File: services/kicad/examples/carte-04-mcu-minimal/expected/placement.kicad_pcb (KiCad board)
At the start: 2 copper layers, 60 x 45 mm, 15 parts, among them J1 IN_5V, J2 SWD, U1 STM32F103C8T6, U2 AMS1117-3.3

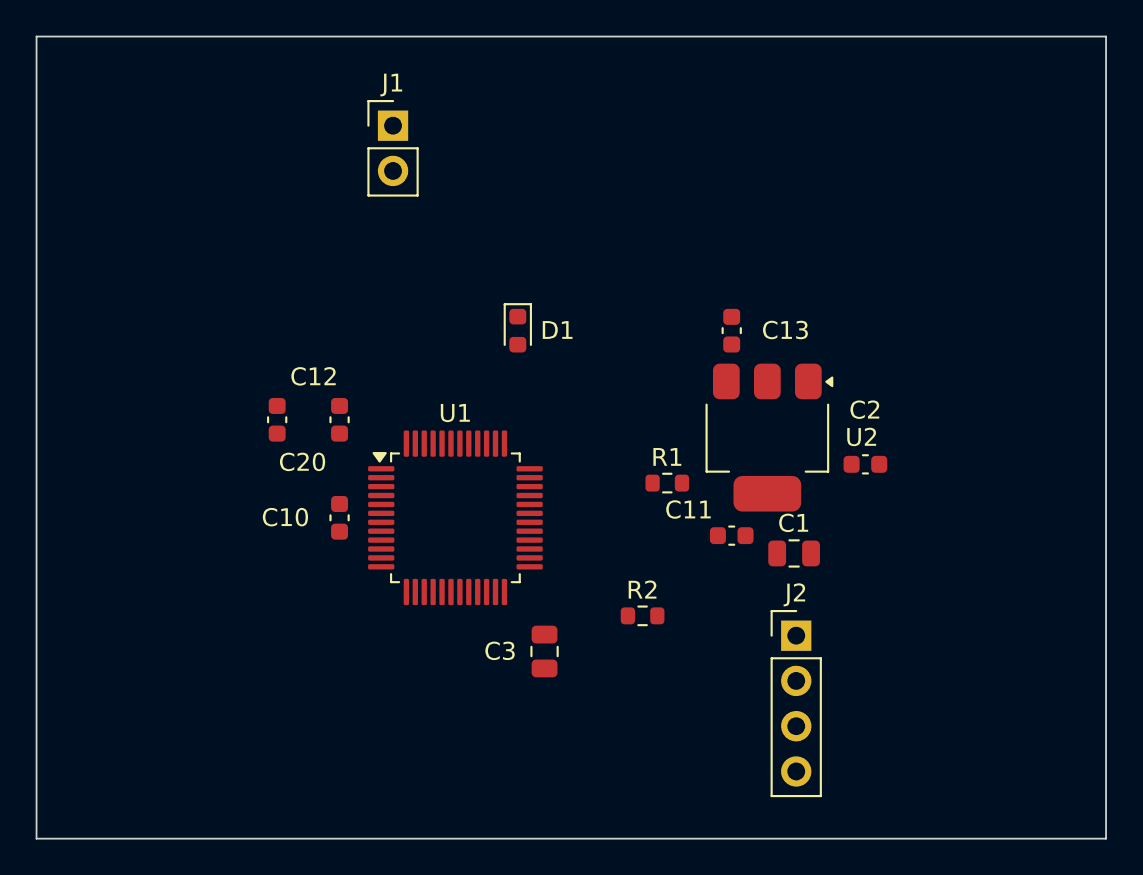
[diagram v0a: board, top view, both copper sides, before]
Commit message: test(examples): quatre cartes livrées plus petites — contour resserré mesuré sur le banc (D-2026-09-13-c A)
Banc rejoué en taille heuristique (phase 1 puis phase 2 à placement gelé) :
carte-01 25x20 -> 24,8x17 (84 % de surface), carte-04 60x45 -> 45x44,8
(75 %), carte-06 80x60 -> 65,2x59,8 (81 %), carte-07 110x80 -> 99,5x79,8
(90 %) — toutes 100 % routées, 0 erreur DRC (vérifié en local), rendus 3D
régénérés. Gain nul sur les cartes denses (le génétique remplit la carte) ;
08 et 09 non livrées (dispersion du routage, surface inchangée) ; carte-11
non livrée (carte d'escalade). Tableau complet dans docs/DECISIONS.md.

Co-Authored-By: Claude Fable 5.1 <noreply@anthropic.com>
Claude-Session: https://claude.ai/code/session_01TnMqm4La2CxQHHB5K8aSSV
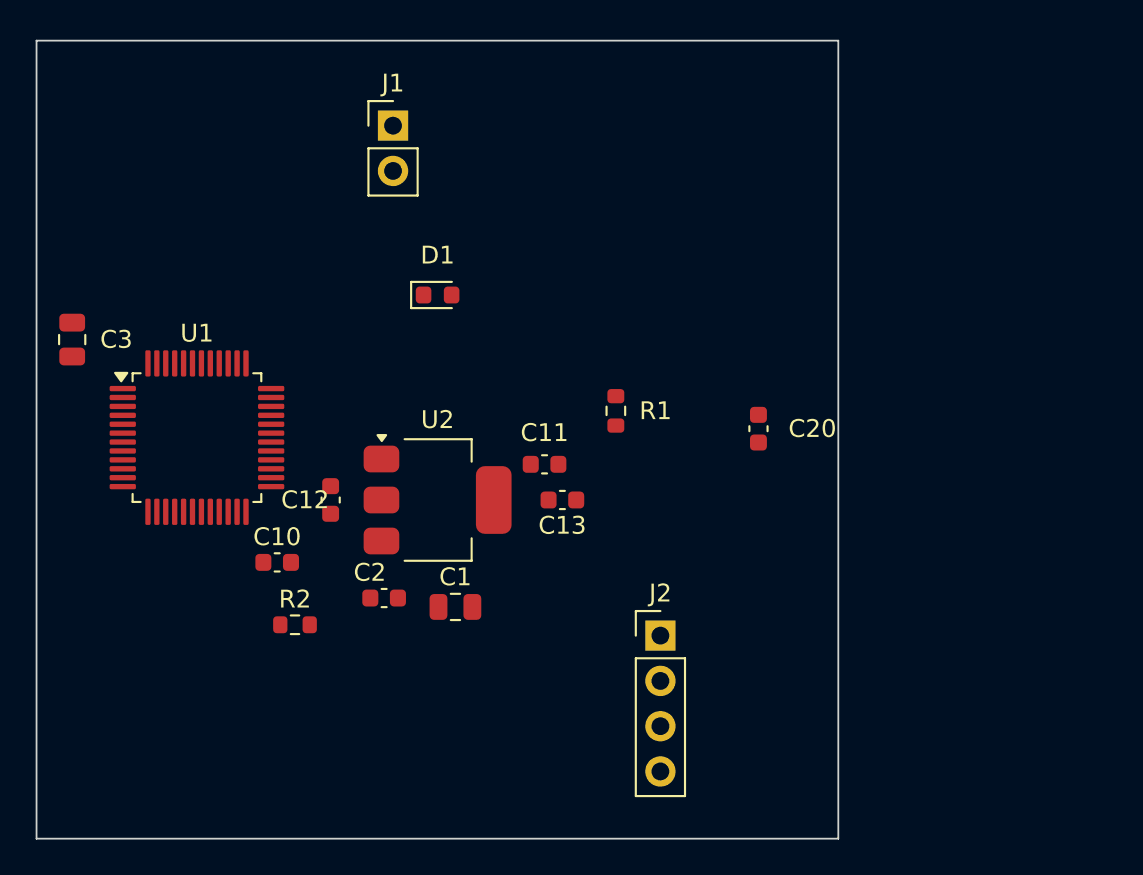
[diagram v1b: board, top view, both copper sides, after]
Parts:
- moved C3 31.8 mm to (120.5, 99.5), turned to 270 degrees
- moved C2 28.0 mm to (138.0, 114.0)
- moved C20 27.0 mm to (159.0, 104.5)
- moved R2 19.5 mm to (133.0, 115.5)
- moved C1 19.2 mm to (142.0, 114.5)
- moved U2 18.8 mm to (141.0, 108.5), turned to 0 degrees
- moved U1 15.2 mm to (127.5, 105.0)
- moved C13 13.4 mm to (148.0, 108.5), turned to 180 degrees
- moved C11 11.2 mm to (147.0, 106.5), turned to 180 degrees
- moved J2 7.62 mm to (153.5, 116.1)
- moved R1 4.97 mm to (151.0, 103.5), turned to 270 degrees
- moved D1 4.92 mm to (141.0, 97.0), turned to 0 degrees
- moved C12 4.53 mm to (135.0, 108.5)
- moved C10 4.30 mm to (132.0, 112.0), turned to 0 degrees
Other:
- board size 60 x 45 mm -> 45 x 44.8 mm
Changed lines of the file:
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@@
 	(title_block
 		(title "Cirqix PCB")
-		(date "2026-09-12")
+		(date "2026-09-13")
 		(rev 1.0)
 		(company "")
@@
 	(net 45 "Net-(U1-12)")
 	(net 46 "Net-(U1-9)")
-	(gr_rect
-		(start 118.5 82.5)
-		(end 178.5 127.5)
-		(stroke
-			(width 0.1)
-			(type default)
-		)
-		(fill none)
-		(layer "Edge.Cuts")
-	)
 	(footprint "LQFP-48_7x7mm_P0.5mm"
 		(version 20260206)
 		(generator "kicad-footprint-generator")
 		(layer "F.Cu")
-		(at 142 109.5 0)
+		(at 127.5 105 0)
 		(descr "LQFP, 48 Pin (JEDEC MS-026 variation BBC, 1.40mm body thickness, https://www.jedec.org/document_search?search_api_views_fulltext=MS-026, https://www.analog.com/media/en/package-pcb-resources/package/pkg_pdf/ltc-legacy-lqfp/05081760_a_lx48.pdf)")
 		(tags "LQFP QFP CASE-932AA CASE-932-03 C48-1 C48-2 C48-3 C48-5 C48-6 C48-6C PT0048A")
@@
 		(generator_version "10.0")
 		(layer "F.Cu")
-		(at 159.5 105 270)
+		(at 141 108.5 0)
 		(descr "module CMS SOT223 4 pins")
 		(tags "CMS SOT")
 		(property "Reference" "U2"
-			(at -1.46958e-16 -5.3 0)
+			(at 0 -4.5 0)
 			(layer "F.SilkS")
 			(effects
@@
 		)
 		(pad "1" smd roundrect
-			(at -3.15 -2.3 270)
+			(at -3.15 -2.3)
 			(size 2 1.5)
 			(layers "F.Cu" "F.Mask" "F.Paste")
@@
 		)
 		(pad "2" smd roundrect
-			(at -3.15 0 270)
+			(at -3.15 0)
 			(size 2 1.5)
 			(layers "F.Cu" "F.Mask" "F.Paste")
@@
 		)
 		(pad "2" smd roundrect
-			(at 3.15 0 270)
+			(at 3.15 0)
 			(size 2 3.8)
 			(layers "F.Cu" "F.Mask" "F.Paste")
@@
 		)
 		(pad "3" smd roundrect
-			(at -3.15 2.3 270)
+			(at -3.15 2.3)
 			(size 2 1.5)
 			(layers "F.Cu" "F.Mask" "F.Paste")
@@
 		(generator "kicad-footprint-generator")
 		(layer "F.Cu")
-		(at 161 111.5 0)
+		(at 142 114.5 0)
 		(descr "Capacitor SMD 0805 (2012 Metric), square (rectangular) end terminal, IPC-7351 nominal, (Body size source: IPC-SM-782 page 76, https://www.pcb-3d.com/wordpress/wp-content/uploads/ipc-sm-782a_amendment_1_and_2.pdf, https://docs.google.com/spreadsheets/d/1BsfQQcO9C6DZCsRaXUlFlo91Tg2WpOkGARC1WS5S8t0/edit?usp=sharing)")
 		(tags "capacitor")
@@
 		(generator "kicad-footprint-generator")
 		(layer "F.Cu")
-		(at 165 106.5 0)
+		(at 138 114 0)
 		(descr "Capacitor SMD 0603 (1608 Metric), square (rectangular) end terminal, IPC-7351 nominal, (Body size source: IPC-SM-782 page 76, https://www.pcb-3d.com/wordpress/wp-content/uploads/ipc-sm-782a_amendment_1_and_2.pdf)")
 		(tags "capacitor")
 		(property "Reference" "C2"
-			(at -2.93915e-16 -3.03 0)
+			(at -0.8 -1.43 0)
 			(layer "F.SilkS")
 			(effects
@@
 		(generator "kicad-footprint-generator")
 		(layer "F.Cu")
-		(at 147 117 90)
+		(at 120.5 99.5 270)
 		(descr "Capacitor SMD 0805 (2012 Metric), square (rectangular) end terminal, IPC-7351 nominal, (Body size source: IPC-SM-782 page 76, https://www.pcb-3d.com/wordpress/wp-content/uploads/ipc-sm-782a_amendment_1_and_2.pdf, https://docs.google.com/spreadsheets/d/1BsfQQcO9C6DZCsRaXUlFlo91Tg2WpOkGARC1WS5S8t0/edit?usp=sharing)")
 		(tags "capacitor")
@@
 		)
 		(pad "1" smd roundrect
-			(at -0.95 0 90)
+			(at -0.95 0 270)
 			(size 1 1.45)
 			(layers "F.Cu" "F.Mask" "F.Paste")
@@
 		)
 		(pad "2" smd roundrect
-			(at 0.95 0 90)
+			(at 0.95 0 270)
 			(size 1 1.45)
 			(layers "F.Cu" "F.Mask" "F.Paste")
@@
 		(generator "kicad-footprint-generator")
 		(layer "F.Cu")
-		(at 153.8862 107.5517 0)
+		(at 151 103.5 270)
 		(descr "Resistor SMD 0603 (1608 Metric), square (rectangular) end terminal, IPC-7351 nominal, (Body size source: IPC-SM-782 page 72, https://www.pcb-3d.com/wordpress/wp-content/uploads/ipc-sm-782a_amendment_1_and_2.pdf)")
 		(tags "resistor")
 		(property "Reference" "R1"
-			(at 0 -1.43 0)
+			(at -1.46958e-16 -2.23 0)
 			(layer "F.SilkS")
 			(effects
@@
 		)
 		(pad "1" smd roundrect
-			(at -0.825 0)
+			(at -0.825 0 270)
 			(size 0.8 0.95)
 			(layers "F.Cu" "F.Mask" "F.Paste")
@@
 		)
 		(pad "2" smd roundrect
-			(at 0.825 0)
+			(at 0.825 0 270)
 			(size 0.8 0.95)
 			(layers "F.Cu" "F.Mask" "F.Paste")
@@
 		(generator "kicad-footprint-generator")
 		(layer "F.Cu")
-		(at 145.5 99 270)
+		(at 141 97 0)
 		(descr "LED SMD 0603 (1608 Metric), square (rectangular) end terminal, IPC-7351 nominal, (Body size source: http://www.tortai-tech.com/upload/download/2011102023233369053.pdf)")
 		(tags "LED")
@@
 		)
 		(pad "1" smd roundrect
-			(at -0.7875 0 270)
+			(at -0.7875 0)
 			(size 0.875 0.95)
 			(layers "F.Cu" "F.Mask" "F.Paste")
@@
 		)
 		(pad "2" smd roundrect
-			(at 0.7875 0 270)
+			(at 0.7875 0)
 			(size 0.875 0.95)
 			(layers "F.Cu" "F.Mask" "F.Paste")
@@
 		(generator "kicad-footprint-generator")
 		(layer "F.Cu")
-		(at 135.5 109.5 90)
+		(at 132 112 0)
 		(descr "Capacitor SMD 0603 (1608 Metric), square (rectangular) end terminal, IPC-7351 nominal, (Body size source: IPC-SM-782 page 76, https://www.pcb-3d.com/wordpress/wp-content/uploads/ipc-sm-782a_amendment_1_and_2.pdf)")
 		(tags "capacitor")
 		(property "Reference" "C10"
-			(at -2.93915e-16 -3.03 0)
+			(at 0 -1.43 0)
 			(layer "F.SilkS")
 			(effects
@@
 		)
 		(pad "1" smd roundrect
-			(at -0.775 0 90)
+			(at -0.775 0)
 			(size 0.9 0.95)
 			(layers "F.Cu" "F.Mask" "F.Paste")
@@
 		)
 		(pad "2" smd roundrect
-			(at 0.775 0 90)
+			(at 0.775 0)
 			(size 0.9 0.95)
 			(layers "F.Cu" "F.Mask" "F.Paste")
@@
 		(generator "kicad-footprint-generator")
 		(layer "F.Cu")
-		(at 157.5 110.5 0)
+		(at 147 106.5 180)
 		(descr "Capacitor SMD 0603 (1608 Metric), square (rectangular) end terminal, IPC-7351 nominal, (Body size source: IPC-SM-782 page 76, https://www.pcb-3d.com/wordpress/wp-content/uploads/ipc-sm-782a_amendment_1_and_2.pdf)")
 		(tags "capacitor")
 		(property "Reference" "C11"
-			(at -2.4 -1.43 0)
+			(at 1.95943e-16 1.77 0)
 			(layer "F.SilkS")
 			(effects
@@
 		)
 		(pad "1" smd roundrect
-			(at -0.775 0)
+			(at -0.775 0 180)
 			(size 0.9 0.95)
 			(layers "F.Cu" "F.Mask" "F.Paste")
@@
 		)
 		(pad "2" smd roundrect
-			(at 0.775 0)
+			(at 0.775 0 180)
 			(size 0.9 0.95)
 			(layers "F.Cu" "F.Mask" "F.Paste")
@@
 		(generator "kicad-footprint-generator")
 		(layer "F.Cu")
-		(at 135.5 104 90)
+		(at 135 108.5 90)
 		(descr "Capacitor SMD 0603 (1608 Metric), square (rectangular) end terminal, IPC-7351 nominal, (Body size source: IPC-SM-782 page 76, https://www.pcb-3d.com/wordpress/wp-content/uploads/ipc-sm-782a_amendment_1_and_2.pdf)")
 		(tags "capacitor")
 		(property "Reference" "C12"
-			(at 2.4 -1.43 0)
+			(at 0 -1.43 0)
 			(layer "F.SilkS")
 			(effects
@@
 		(generator "kicad-footprint-generator")
 		(layer "F.Cu")
-		(at 157.5 99 270)
+		(at 148 108.5 180)
 		(descr "Capacitor SMD 0603 (1608 Metric), square (rectangular) end terminal, IPC-7351 nominal, (Body size source: IPC-SM-782 page 76, https://www.pcb-3d.com/wordpress/wp-content/uploads/ipc-sm-782a_amendment_1_and_2.pdf)")
 		(tags "capacitor")
 		(property "Reference" "C13"
-			(at -2.93915e-16 -3.03 0)
+			(at 0 -1.43 0)
 			(layer "F.SilkS")
 			(effects
@@
 		)
 		(pad "1" smd roundrect
-			(at -0.775 0 270)
+			(at -0.775 0 180)
 			(size 0.9 0.95)
 			(layers "F.Cu" "F.Mask" "F.Paste")
@@
 		)
 		(pad "2" smd roundrect
-			(at 0.775 0 270)
+			(at 0.775 0 180)
 			(size 0.9 0.95)
 			(layers "F.Cu" "F.Mask" "F.Paste")
@@
 		(generator "kicad-footprint-generator")
 		(layer "F.Cu")
-		(at 152.5 115 0)
+		(at 133 115.5 0)
 		(descr "Resistor SMD 0603 (1608 Metric), square (rectangular) end terminal, IPC-7351 nominal, (Body size source: IPC-SM-782 page 72, https://www.pcb-3d.com/wordpress/wp-content/uploads/ipc-sm-782a_amendment_1_and_2.pdf)")
 		(tags "resistor")
@@
 		(generator "kicad-footprint-generator")
 		(layer "F.Cu")
-		(at 132 104 270)
+		(at 159 104.5 270)
 		(descr "Capacitor SMD 0603 (1608 Metric), square (rectangular) end terminal, IPC-7351 nominal, (Body size source: IPC-SM-782 page 76, https://www.pcb-3d.com/wordpress/wp-content/uploads/ipc-sm-782a_amendment_1_and_2.pdf)")
 		(tags "capacitor")
 		(property "Reference" "C20"
-			(at 2.4 -1.43 0)
+			(at -2.93915e-16 -3.03 0)
 			(layer "F.SilkS")
 			(effects
@@
 		(generator "kicad-footprint-generator")
 		(layer "F.Cu")
-		(at 161.12 116.11 0)
+		(at 153.5 116.11 0)
 		(descr "Through hole straight pin header, 1x04, 2.54mm pitch, single row")
 		(tags "Through hole pin header THT 1x04 2.54mm single row")
@@
 		)
 	)
+	(gr_rect
+		(start 118.500 82.730)
+		(end 163.480 127.500)
+		(stroke
+			(width 0.1)
+			(type default)
+		)
+		(fill no)
+		(layer "Edge.Cuts")
+	)
 )

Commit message: chore(banc): relivrer carte-01/02/04/05 compactes (25 %, D-2026-09-20-a) (#222)
Chaine place -> route rejouee par HTTP sur les dix cartes avec le code de
#220/#221. Quatre sortent a 0 erreur et 0 connexion manquante, sur des
cartes 18 a 58 % plus petites :

  carte-01  24,8x17 -> 20x14      carte-02  55x40 -> 35x25
  carte-04  45x44,8 -> 39x30      carte-05  70x50 -> 46x33

placement.kicad_pcb et final.kicad_pcb remplaces ENSEMBLE ; mesures.json :
board recompte, drc_du_board rejuge (remesurer_banc.py), cle
carte_compacte (tailles et vias d avant, durees, moteur, pistes par
couche). Rendus refaits. Connecteurs a <= 5 mm d un bord (carte-02 J2 :
13,9 -> 3,8 mm) ; carte-05 J3 inchange a 11,4 mm (origine pin 1).

Les six autres gardent leur board du 2026-09-19 : 06 et 08 a 1 manquante,
03 et 07 mauvais, 09 et 10 sans board (tirages figes). Detail dans
BANC_DRIVER_LLM.md. carte-11 non touchee.


Claude-Session: https://claude.ai/code/session_01TnMqm4La2CxQHHB5K8aSSV

Co-authored-by: Claude Fable 5.1 <noreply@anthropic.com>
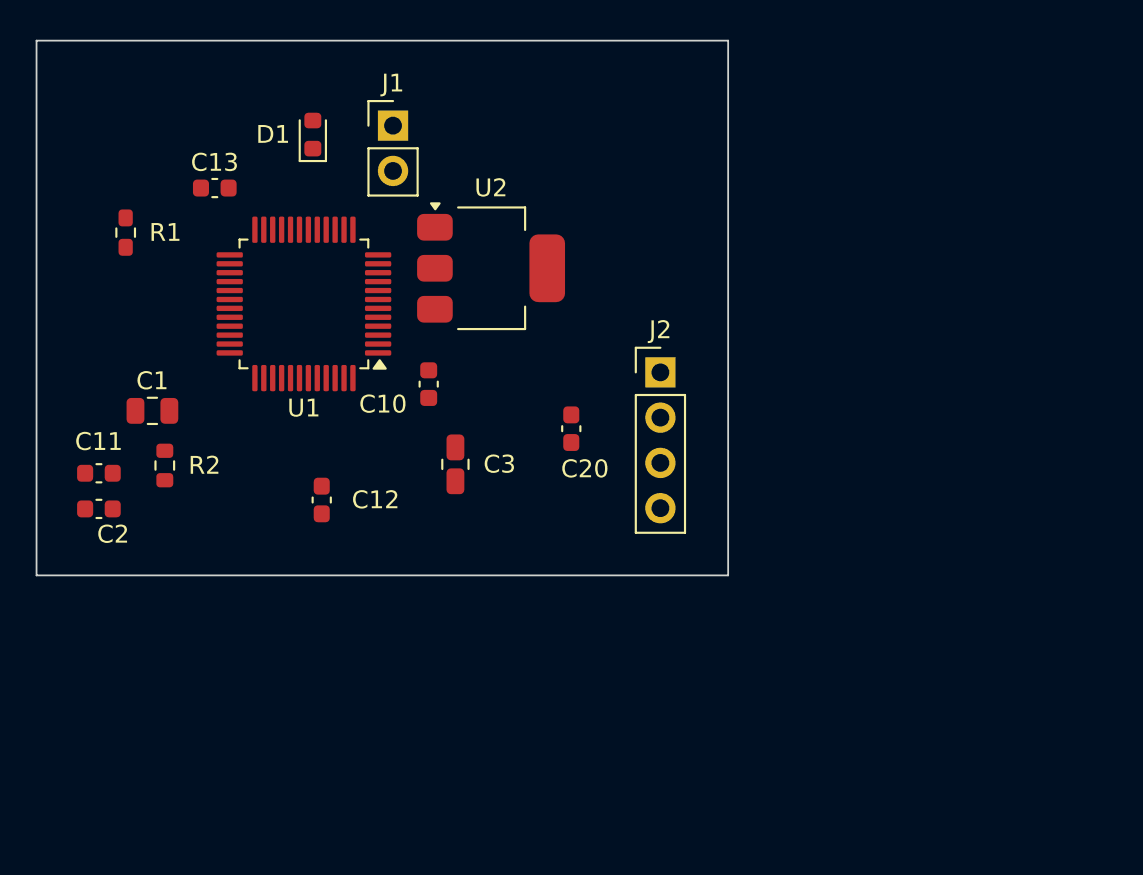
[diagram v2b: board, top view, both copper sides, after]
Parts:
- moved R1 29.3 mm to (123.5, 93.5)
- moved C13 26.2 mm to (128.5, 91.0), turned to 0 degrees
- moved C11 25.0 mm to (122.0, 107.0)
- moved C3 22.6 mm to (142.0, 106.5)
- moved C1 20.2 mm to (125.0, 103.5)
- moved C2 16.8 mm to (122.0, 109.0), turned to 180 degrees
- moved J2 14.8 mm to (153.5, 101.3)
- moved U2 13.3 mm to (144.0, 95.5)
- moved C10 13.1 mm to (140.5, 102.0), turned to 90 degrees
- moved R2 11.5 mm to (125.7, 106.6), turned to 270 degrees
- moved D1 11.4 mm to (134.0, 88.0), turned to 90 degrees
- moved C20 10.5 mm to (148.5, 104.5)
- moved U1 9.60 mm to (133.5, 97.5), turned to 180 degrees
- moved C12 0.50 mm to (134.5, 108.5), turned to 270 degrees
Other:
- board size 45 x 44.8 mm -> 38.8 x 30 mm
